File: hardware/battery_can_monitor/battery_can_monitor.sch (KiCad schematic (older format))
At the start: 71 parts, among them J1 sense3, J10 int, J11 GPIO, J12 GPIO, J13 power, J14 CAN_PWR, J15 CANGND, J2 sense1, J3 Conn_01x05_Male, J4 RJ45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

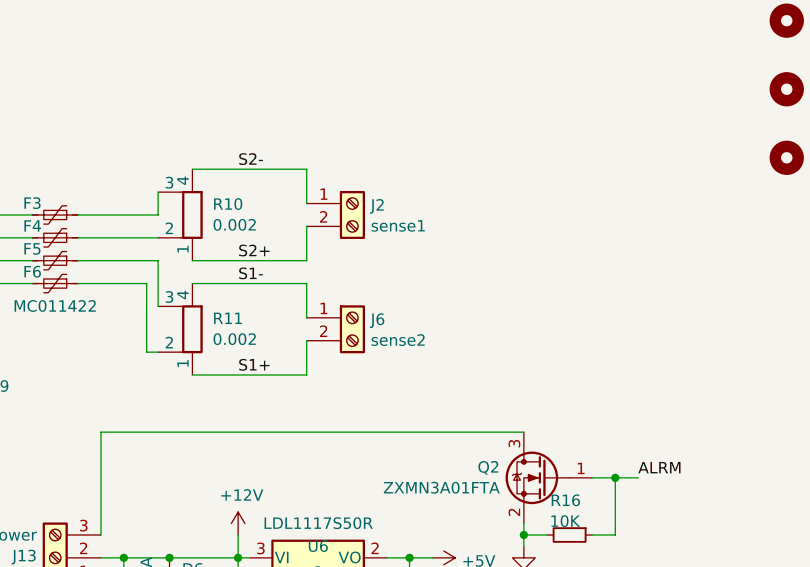
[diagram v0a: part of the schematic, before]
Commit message: Fix name of connectors (sense1/sense2 swapped)
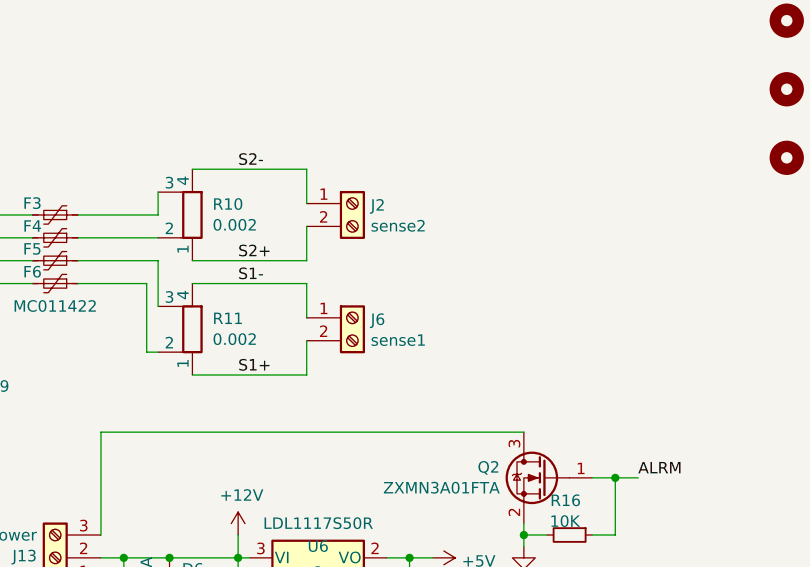
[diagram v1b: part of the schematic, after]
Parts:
- J2: value sense1 -> sense2
- J6: value sense2 -> sense1
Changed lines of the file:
@@
 P 8100 2150
 F 0 "J2" H 8180 2142 50  0000 L CNN
-F 1 "sense1" H 8180 2051 50  0000 L CNN
+F 1 "sense2" H 8180 2051 50  0000 L CNN
 F 2 "TerminalBlock_MetzConnect:TerminalBlock_MetzConnect_Type703_RT10N02HGLU_1x02_P9.52mm_Horizontal" H 8100 2150 50  0001 C CNN
 F 3 "~" H 8100 2150 50  0001 C CNN
@@
 P 8100 2650
 F 0 "J6" H 8180 2642 50  0000 L CNN
-F 1 "sense2" H 8180 2551 50  0000 L CNN
+F 1 "sense1" H 8180 2551 50  0000 L CNN
 F 2 "TerminalBlock_MetzConnect:TerminalBlock_MetzConnect_Type703_RT10N02HGLU_1x02_P9.52mm_Horizontal" H 8100 2650 50  0001 C CNN
 F 3 "~" H 8100 2650 50  0001 C CNN
